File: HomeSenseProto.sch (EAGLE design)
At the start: 22 parts, among them IC1 ESP12SMT

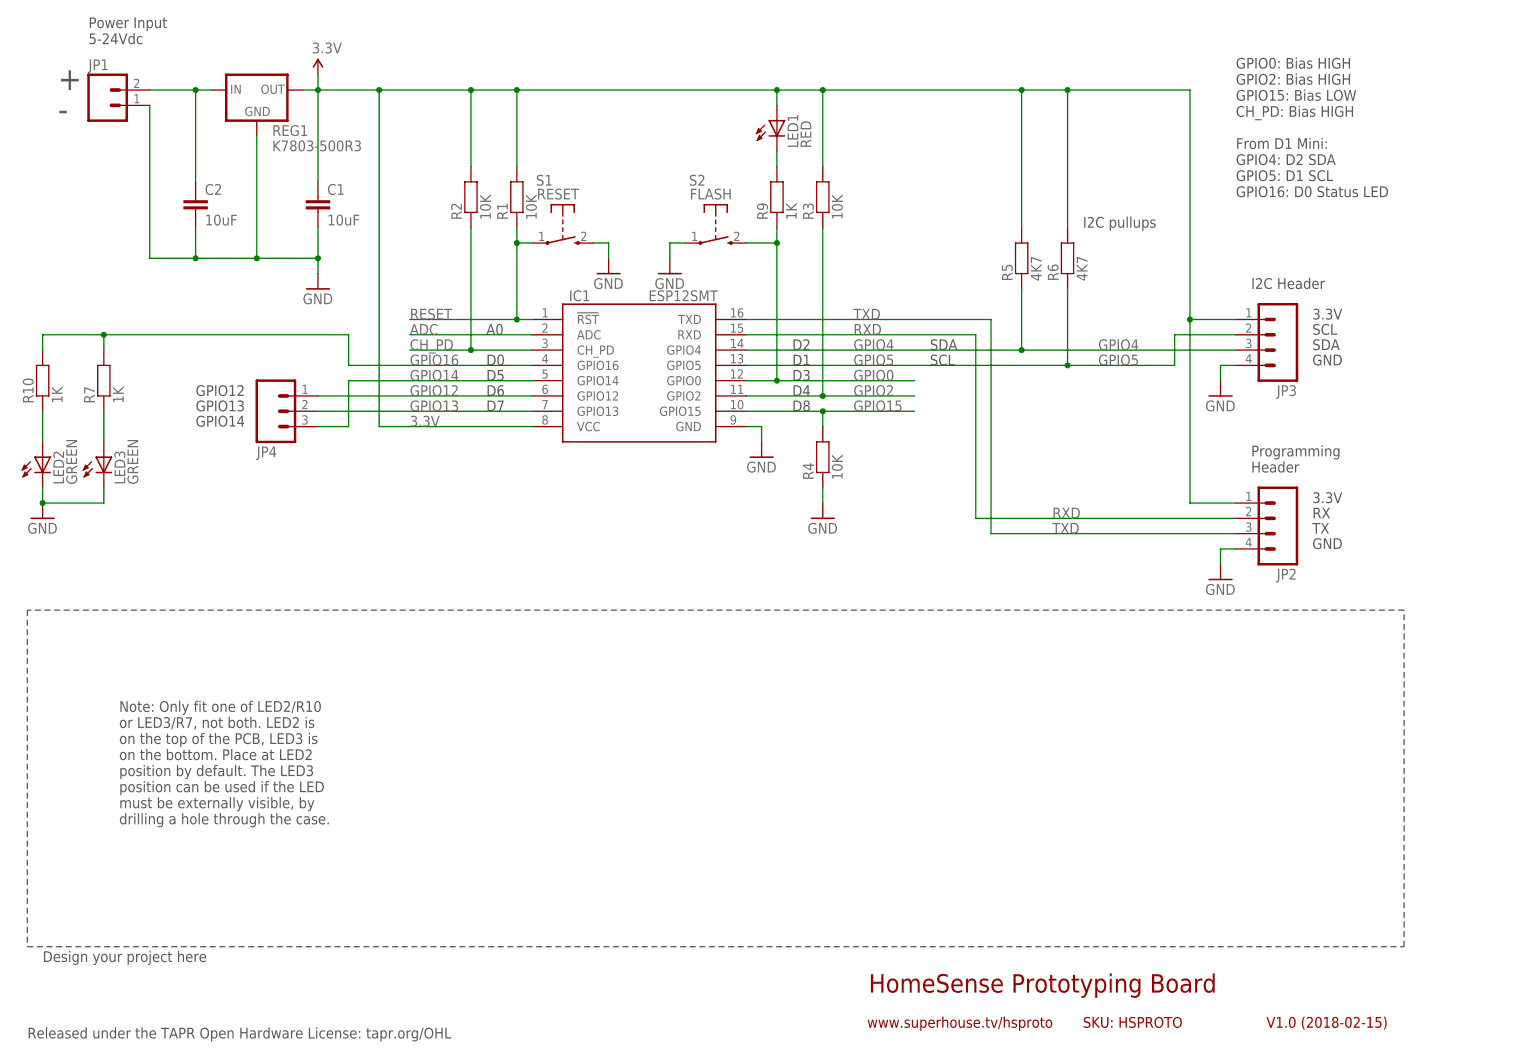
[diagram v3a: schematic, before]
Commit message: Updated routing and schematic for v1.0 release
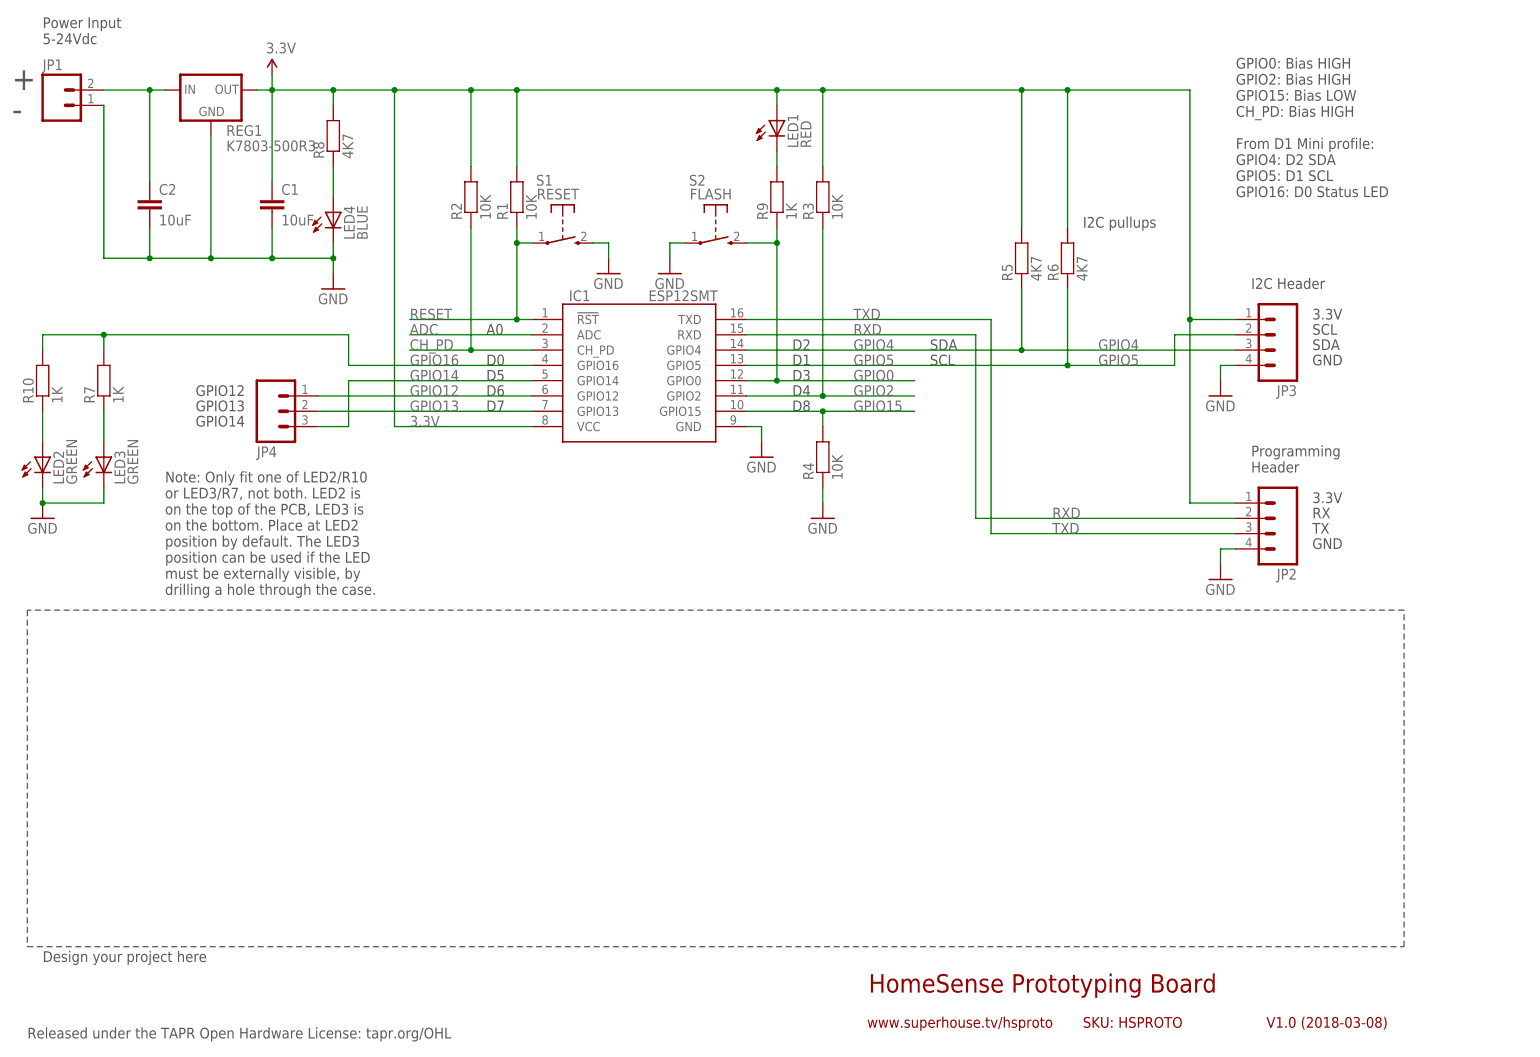
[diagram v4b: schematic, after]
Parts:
- added LED4: BLUE, freetronics-jon:LED0603
- added R8: 4K7, freetronics-jon:RESISTOR0603
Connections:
- new net N$65: LED4.A, R8.1
- net 3.3V: now also R8.2
- net GND: now also LED4.C
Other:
- note added: "GPIO0: Bias HIGH GPIO2: Bias HIGH GPIO15: Bias LOW CH_PD: Bias HIGH From D1 Mini profile: GPIO4: D2 SDA GPIO5: D1 SCL GPIO16: D0 Status LED"
- note added: "V1.0 (2018-03-08)"
- note removed: "GPIO0: Bias HIGH GPIO2: Bias HIGH GPIO15: Bias LOW CH_PD: Bias HIGH From D1 Mini: GPIO4: D2 SDA GPIO5: D1 SCL GPIO16: D0 Status LED"
- note removed: "V1.0 (2018-02-15)"
- moved on the sheet: C1, C2, JP1, REG1
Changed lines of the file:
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@@
 <part name="GND5" library="freetronics-original" deviceset="GND" device=""/>
 <part name="C1" library="freetronics-jon" deviceset="CAP" device="0805" value="10uF"/>
-<part name="GND6" library="freetronics-original" deviceset="GND" device=""/>
 <part name="GND7" library="freetronics-original" deviceset="GND" device=""/>
 <part name="R5" library="freetronics-jon" deviceset="RESISTOR" device="0603" value="4K7"/>
@@
 <part name="R7" library="freetronics-jon" deviceset="RESISTOR" device="0603" value="1K"/>
 <part name="JP4" library="freetronics-jon" deviceset="M03" device="PTH"/>
+<part name="LED4" library="freetronics-jon" deviceset="LED" device="0603" value="BLUE"/>
+<part name="R8" library="freetronics-jon" deviceset="RESISTOR" device="0603" value="4K7"/>
+<part name="GND8" library="freetronics-original" deviceset="GND" device=""/>
 </parts>
 <sheets>
@@
 <plain>
 <text x="149.86" y="12.7" size="3.048" layer="94">HomeSense Prototyping Board</text>
-<text x="215.9" y="6.858" size="1.778" layer="94">V1.0 (2018-02-15)</text>
+<text x="215.9" y="6.858" size="1.778" layer="94">V1.0 (2018-03-08)</text>
 <text x="149.606" y="6.858" size="1.778" layer="94">www.superhouse.tv/hsproto</text>
 <frame x1="0" y1="0" x2="248.92" y2="185.42" columns="8" rows="5" layer="94"/>
@@
 GPIO15: Bias LOW
 CH_PD: Bias HIGH
-From D1 Mini:
+From D1 Mini profile:
 GPIO4: D2 SDA
 GPIO5: D1 SCL
@@
 <text x="223.52" y="88.9" size="1.778" layer="97">TX</text>
 <text x="223.52" y="86.36" size="1.778" layer="97">GND</text>
-<text x="20.32" y="170.18" size="1.778" layer="97">Power Input
+<text x="12.7" y="170.18" size="1.778" layer="97">Power Input
 5-24Vdc</text>
-<text x="15.24" y="162.56" size="3.81" layer="97">+</text>
-<text x="15.24" y="157.48" size="3.81" layer="97">-</text>
+<text x="7.62" y="162.56" size="3.81" layer="97">+</text>
+<text x="7.62" y="157.48" size="3.81" layer="97">-</text>
 <text x="223.52" y="124.46" size="1.778" layer="97">3.3V</text>
 <text x="223.52" y="119.38" size="1.778" layer="97">SDA</text>
@@
 <wire x1="238.76" y1="76.2" x2="10.16" y2="76.2" width="0.1524" layer="97" style="longdash"/>
 <wire x1="10.16" y1="76.2" x2="10.16" y2="20.32" width="0.1524" layer="97" style="longdash"/>
-<text x="25.4" y="40.64" size="1.778" layer="97">Note: Only fit one of LED2/R10
+<text x="33.02" y="78.74" size="1.778" layer="97">Note: Only fit one of LED2/R10
 or LED3/R7, not both. LED2 is
 on the top of the PCB, LED3 is
@@
 <instance part="GND4" gate="1" x="132.08" y="101.6"/>
 <instance part="R1" gate="G$1" x="91.44" y="144.78" rot="R90"/>
-<instance part="P+2" gate="G$1" x="58.42" y="165.1"/>
+<instance part="P+2" gate="G$1" x="50.8" y="165.1"/>
 <instance part="R2" gate="G$1" x="83.82" y="144.78" rot="R90"/>
 <instance part="R3" gate="G$1" x="142.24" y="144.78" rot="R90"/>
 <instance part="R4" gate="G$1" x="142.24" y="101.6" rot="R90"/>
 <instance part="GND5" gate="1" x="142.24" y="91.44"/>
-<instance part="C1" gate="G$1" x="58.42" y="142.24"/>
-<instance part="GND6" gate="1" x="58.42" y="129.54"/>
+<instance part="C1" gate="G$1" x="50.8" y="142.24"/>
 <instance part="GND7" gate="1" x="208.28" y="111.76"/>
 <instance part="R5" gate="G$1" x="175.26" y="134.62" rot="R90"/>
@@
 <instance part="LED1" gate="G$1" x="134.62" y="157.48"/>
 <instance part="R9" gate="G$1" x="134.62" y="144.78" rot="R90"/>
-<instance part="C2" gate="G$1" x="38.1" y="142.24"/>
+<instance part="C2" gate="G$1" x="30.48" y="142.24"/>
 <instance part="R10" gate="G$1" x="12.7" y="114.3" rot="R90"/>
 <instance part="LED2" gate="G$1" x="12.7" y="101.6"/>
 <instance part="GND11" gate="1" x="12.7" y="91.44"/>
-<instance part="JP1" gate="G$1" x="22.86" y="160.02"/>
+<instance part="JP1" gate="G$1" x="15.24" y="160.02"/>
 <instance part="JP2" gate="G$1" x="215.9" y="91.44" rot="R180"/>
 <instance part="S2" gate="1" x="124.46" y="137.16"/>
 <instance part="GND1" gate="1" x="208.28" y="81.28"/>
-<instance part="REG1" gate="G$1" x="48.26" y="162.56"/>
+<instance part="REG1" gate="G$1" x="40.64" y="162.56"/>
 <instance part="GND2" gate="1" x="116.84" y="132.08"/>
 <instance part="JP3" gate="G$1" x="215.9" y="121.92" rot="R180"/>
@@
 <instance part="R7" gate="G$1" x="22.86" y="114.3" rot="R90"/>
 <instance part="JP4" gate="G$1" x="50.8" y="109.22" rot="MR180"/>
+<instance part="LED4" gate="G$1" x="60.96" y="142.24"/>
+<instance part="R8" gate="G$1" x="60.96" y="154.94" rot="R90"/>
+<instance part="GND8" gate="1" x="60.96" y="129.54"/>
 </instances>
 <busses>
@@
 <segment>
 <pinref part="C2" gate="G$1" pin="2"/>
-<wire x1="38.1" y1="139.7" x2="38.1" y2="134.62" width="0.1524" layer="91"/>
+<wire x1="30.48" y1="139.7" x2="30.48" y2="134.62" width="0.1524" layer="91"/>
 <pinref part="JP1" gate="G$1" pin="1"/>
-<wire x1="30.48" y1="160.02" x2="30.48" y2="134.62" width="0.1524" layer="91"/>
-<wire x1="30.48" y1="134.62" x2="38.1" y2="134.62" width="0.1524" layer="91"/>
-<junction x="38.1" y="134.62"/>
-<wire x1="48.26" y1="154.94" x2="48.26" y2="134.62" width="0.1524" layer="91"/>
-<wire x1="38.1" y1="134.62" x2="48.26" y2="134.62" width="0.1524" layer="91"/>
-<junction x="48.26" y="134.62"/>
+<wire x1="22.86" y1="160.02" x2="22.86" y2="134.62" width="0.1524" layer="91"/>
+<wire x1="22.86" y1="134.62" x2="30.48" y2="134.62" width="0.1524" layer="91"/>
+<junction x="30.48" y="134.62"/>
+<wire x1="40.64" y1="154.94" x2="40.64" y2="134.62" width="0.1524" layer="91"/>
+<wire x1="30.48" y1="134.62" x2="40.64" y2="134.62" width="0.1524" layer="91"/>
+<junction x="40.64" y="134.62"/>
 <pinref part="C1" gate="G$1" pin="2"/>
-<pinref part="GND6" gate="1" pin="GND"/>
-<wire x1="58.42" y1="139.7" x2="58.42" y2="134.62" width="0.1524" layer="91"/>
-<wire x1="58.42" y1="134.62" x2="58.42" y2="132.08" width="0.1524" layer="91"/>
-<wire x1="48.26" y1="134.62" x2="58.42" y2="134.62" width="0.1524" layer="91"/>
-<junction x="58.42" y="134.62"/>
+<wire x1="50.8" y1="139.7" x2="50.8" y2="134.62" width="0.1524" layer="91"/>
+<wire x1="40.64" y1="134.62" x2="50.8" y2="134.62" width="0.1524" layer="91"/>
+<junction x="50.8" y="134.62"/>
 <pinref part="REG1" gate="G$1" pin="GND"/>
+<wire x1="50.8" y1="134.62" x2="60.96" y2="134.62" width="0.1524" layer="91"/>
+<pinref part="LED4" gate="G$1" pin="C"/>
+<wire x1="60.96" y1="134.62" x2="60.96" y2="137.16" width="0.1524" layer="91"/>
+<pinref part="GND8" gate="1" pin="GND"/>
+<wire x1="60.96" y1="132.08" x2="60.96" y2="134.62" width="0.1524" layer="91"/>
+<junction x="60.96" y="134.62"/>
 </segment>
 <segment>
@@
 <wire x1="210.82" y1="93.98" x2="203.2" y2="93.98" width="0.1524" layer="91"/>
 <pinref part="P+2" gate="G$1" pin="3.3V"/>
-<wire x1="55.88" y1="162.56" x2="58.42" y2="162.56" width="0.1524" layer="91"/>
-<wire x1="58.42" y1="162.56" x2="58.42" y2="165.1" width="0.1524" layer="91"/>
+<wire x1="48.26" y1="162.56" x2="50.8" y2="162.56" width="0.1524" layer="91"/>
+<wire x1="50.8" y1="162.56" x2="50.8" y2="165.1" width="0.1524" layer="91"/>
 <pinref part="IC1" gate="G$1" pin="VCC"/>
-<wire x1="93.98" y1="106.68" x2="68.58" y2="106.68" width="0.1524" layer="91"/>
-<wire x1="68.58" y1="106.68" x2="68.58" y2="162.56" width="0.1524" layer="91"/>
+<wire x1="93.98" y1="106.68" x2="71.12" y2="106.68" width="0.1524" layer="91"/>
+<wire x1="71.12" y1="106.68" x2="71.12" y2="162.56" width="0.1524" layer="91"/>
 <pinref part="C1" gate="G$1" pin="1"/>
-<wire x1="58.42" y1="162.56" x2="68.58" y2="162.56" width="0.1524" layer="91"/>
-<junction x="58.42" y="162.56"/>
-<junction x="68.58" y="162.56"/>
+<wire x1="50.8" y1="162.56" x2="60.96" y2="162.56" width="0.1524" layer="91"/>
+<junction x="50.8" y="162.56"/>
+<junction x="71.12" y="162.56"/>
 <pinref part="R2" gate="G$1" pin="2"/>
+<wire x1="60.96" y1="162.56" x2="71.12" y2="162.56" width="0.1524" layer="91"/>
 <wire x1="83.82" y1="149.86" x2="83.82" y2="162.56" width="0.1524" layer="91"/>
 <junction x="83.82" y="162.56"/>
 <pinref part="R1" gate="G$1" pin="2"/>
-<wire x1="68.58" y1="162.56" x2="83.82" y2="162.56" width="0.1524" layer="91"/>
+<wire x1="71.12" y1="162.56" x2="83.82" y2="162.56" width="0.1524" layer="91"/>
 <wire x1="91.44" y1="149.86" x2="91.44" y2="162.56" width="0.1524" layer="91"/>
 <wire x1="83.82" y1="162.56" x2="91.44" y2="162.56" width="0.1524" layer="91"/>
@@
 <junction x="182.88" y="162.56"/>
 <wire x1="182.88" y1="162.56" x2="203.2" y2="162.56" width="0.1524" layer="91"/>
-<wire x1="58.42" y1="147.32" x2="58.42" y2="162.56" width="0.1524" layer="91"/>
+<wire x1="50.8" y1="147.32" x2="50.8" y2="162.56" width="0.1524" layer="91"/>
 <pinref part="REG1" gate="G$1" pin="OUT"/>
 <wire x1="142.24" y1="149.86" x2="142.24" y2="162.56" width="0.1524" layer="91"/>
@@
 <wire x1="210.82" y1="124.46" x2="203.2" y2="124.46" width="0.1524" layer="91"/>
 <junction x="203.2" y="124.46"/>
+<pinref part="R8" gate="G$1" pin="2"/>
+<wire x1="60.96" y1="160.02" x2="60.96" y2="162.56" width="0.1524" layer="91"/>
+<junction x="60.96" y="162.56"/>
 </segment>
 </net>
@@
 <net name="N$1" class="0">
 <segment>
-<wire x1="30.48" y1="162.56" x2="38.1" y2="162.56" width="0.1524" layer="91"/>
+<wire x1="22.86" y1="162.56" x2="30.48" y2="162.56" width="0.1524" layer="91"/>
 <pinref part="JP1" gate="G$1" pin="2"/>
 <pinref part="C2" gate="G$1" pin="1"/>
-<wire x1="38.1" y1="162.56" x2="40.64" y2="162.56" width="0.1524" layer="91"/>
-<wire x1="38.1" y1="147.32" x2="38.1" y2="162.56" width="0.1524" layer="91"/>
-<junction x="38.1" y="162.56"/>
+<wire x1="30.48" y1="162.56" x2="33.02" y2="162.56" width="0.1524" layer="91"/>
+<wire x1="30.48" y1="147.32" x2="30.48" y2="162.56" width="0.1524" layer="91"/>
+<junction x="30.48" y="162.56"/>
 <pinref part="REG1" gate="G$1" pin="IN"/>
 </segment>
@@
 </segment>
 </net>
+<net name="N$65" class="0">
+<segment>
+<pinref part="R8" gate="G$1" pin="1"/>
+<pinref part="LED4" gate="G$1" pin="A"/>
+<wire x1="60.96" y1="149.86" x2="60.96" y2="144.78" width="0.1524" layer="91"/>
+</segment>
+</net>
